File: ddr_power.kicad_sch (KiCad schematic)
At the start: 27 parts, among them U2 MT53D512M32D2DS

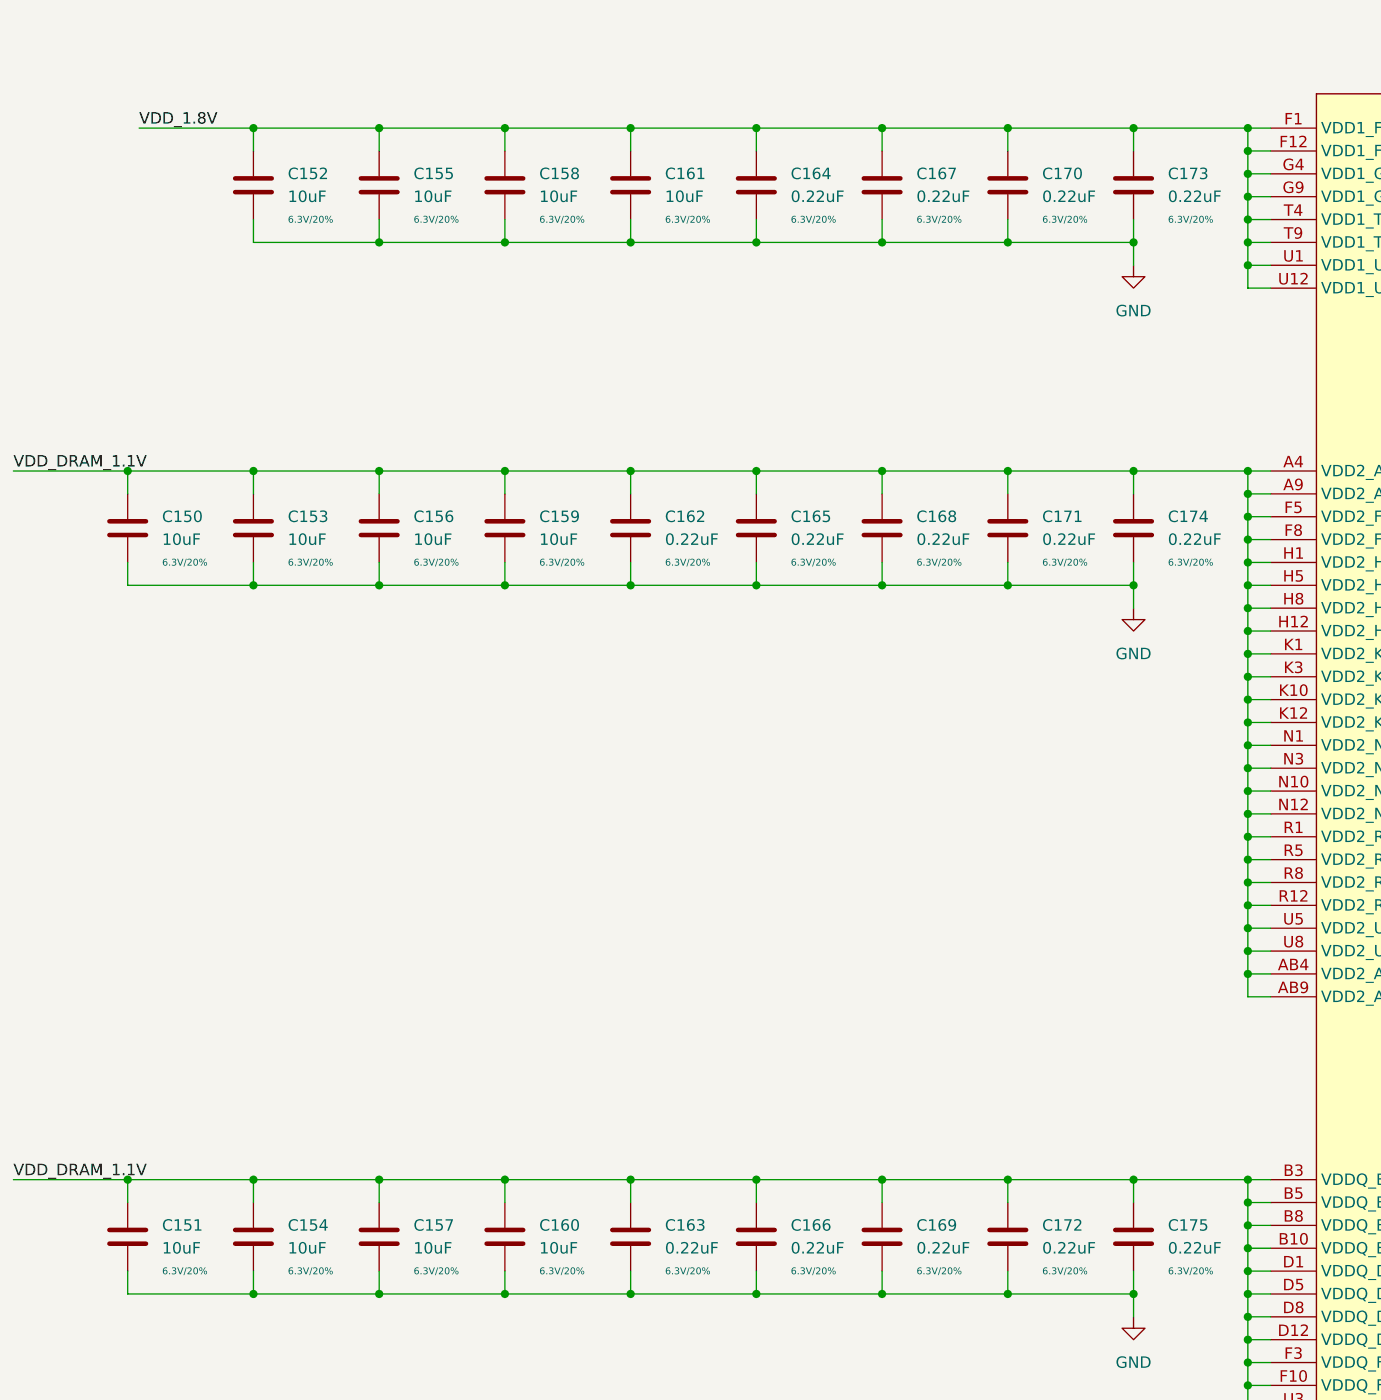
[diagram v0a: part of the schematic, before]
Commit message: add SN65DSI86 DSI2DP ic, SCH, PCB work, flytime work
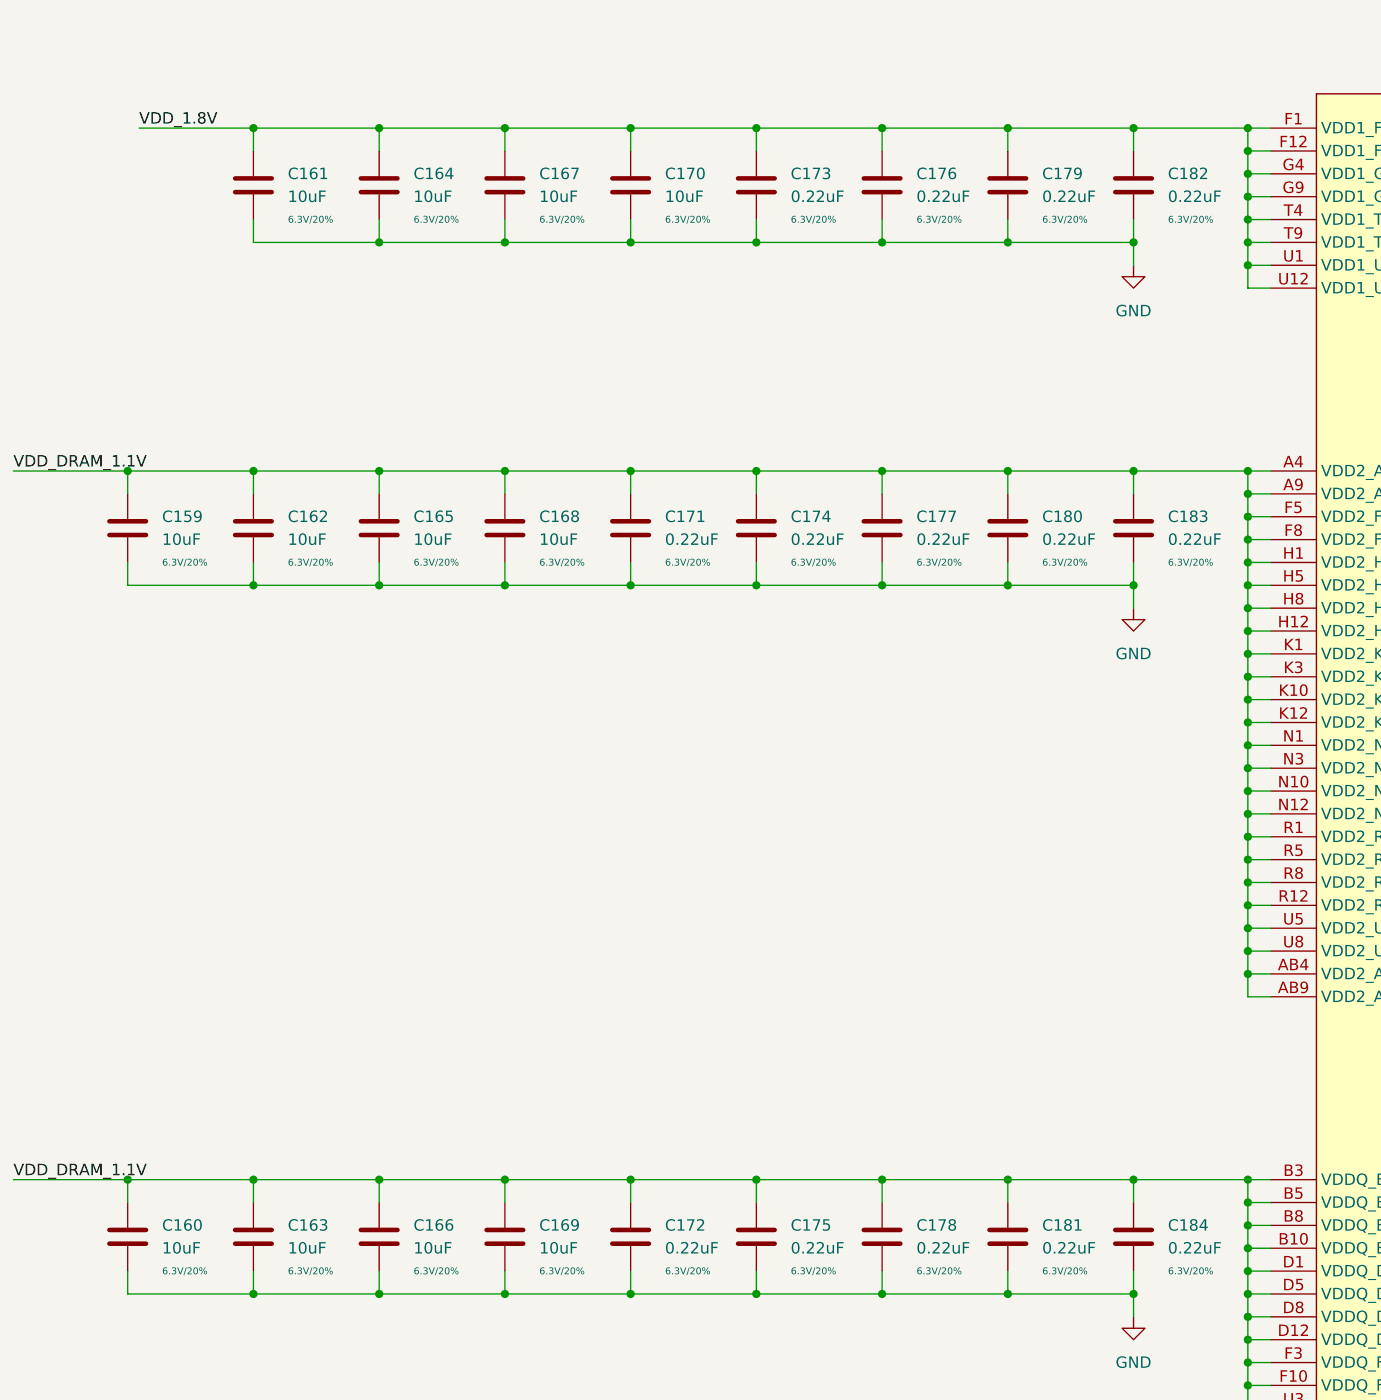
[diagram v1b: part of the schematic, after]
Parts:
- renumbered C150 to C159, C151 to C160, C152 to C161, C153 to C162, C154 to C163, C155 to C164, C156 to C165, C157 to C166, C158 to C167, C159 to C168, C160 to C169, C161 to C170, C162 to C171, C163 to C172, C164 to C173, C165 to C174, C166 to C175, C167 to C176, C168 to C177, C169 to C178, C170 to C179, C171 to C180, C172 to C181, C173 to C182, C174 to C183, C175 to C184
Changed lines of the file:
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@@
   (symbol (lib_id "Device:C") (at 120.65 59.69 0) (unit 1)
     (in_bom yes) (on_board yes)
-    (property "Reference" "C155" (id 0) (at 124.46 58.4199 0)
+    (property "Reference" "C164" (id 0) (at 124.46 58.4199 0)
       (effects (font (size 1.27 1.27)) (justify left))
     )
@@
   (symbol (lib_id "Device:C") (at 190.5 59.69 0) (unit 1)
     (in_bom yes) (on_board yes)
-    (property "Reference" "C170" (id 0) (at 194.31 58.4199 0)
+    (property "Reference" "C179" (id 0) (at 194.31 58.4199 0)
       (effects (font (size 1.27 1.27)) (justify left))
     )
@@
   (symbol (lib_id "Device:C") (at 162.56 97.79 0) (unit 1)
     (in_bom yes) (on_board yes)
-    (property "Reference" "C165" (id 0) (at 166.37 96.5199 0)
+    (property "Reference" "C174" (id 0) (at 166.37 96.5199 0)
       (effects (font (size 1.27 1.27)) (justify left))
     )
@@
   (symbol (lib_id "Device:C") (at 190.5 176.53 0) (unit 1)
     (in_bom yes) (on_board yes)
-    (property "Reference" "C172" (id 0) (at 194.31 175.2599 0)
+    (property "Reference" "C181" (id 0) (at 194.31 175.2599 0)
       (effects (font (size 1.27 1.27)) (justify left))
     )
@@
   (symbol (lib_id "Device:C") (at 148.59 59.69 0) (unit 1)
     (in_bom yes) (on_board yes)
-    (property "Reference" "C161" (id 0) (at 152.4 58.4199 0)
+    (property "Reference" "C170" (id 0) (at 152.4 58.4199 0)
       (effects (font (size 1.27 1.27)) (justify left))
     )
@@
   (symbol (lib_id "Device:C") (at 190.5 97.79 0) (unit 1)
     (in_bom yes) (on_board yes)
-    (property "Reference" "C171" (id 0) (at 194.31 96.5199 0)
+    (property "Reference" "C180" (id 0) (at 194.31 96.5199 0)
       (effects (font (size 1.27 1.27)) (justify left))
     )
@@
   (symbol (lib_id "Device:C") (at 176.53 59.69 0) (unit 1)
     (in_bom yes) (on_board yes)
-    (property "Reference" "C167" (id 0) (at 180.34 58.4199 0)
+    (property "Reference" "C176" (id 0) (at 180.34 58.4199 0)
       (effects (font (size 1.27 1.27)) (justify left))
     )
@@
   (symbol (lib_id "power:GND") (at 204.47 68.58 0) (unit 1)
     (in_bom yes) (on_board yes) (fields_autoplaced)
-    (property "Reference" "#PWR0147" (id 0) (at 204.47 74.93 0)
+    (property "Reference" "#PWR0150" (id 0) (at 204.47 74.93 0)
       (effects (font (size 1.27 1.27)) hide)
     )
@@
   (symbol (lib_id "Device:C") (at 134.62 59.69 0) (unit 1)
     (in_bom yes) (on_board yes)
-    (property "Reference" "C158" (id 0) (at 138.43 58.4199 0)
+    (property "Reference" "C167" (id 0) (at 138.43 58.4199 0)
       (effects (font (size 1.27 1.27)) (justify left))
     )
@@
   (symbol (lib_id "Device:C") (at 204.47 176.53 0) (unit 1)
     (in_bom yes) (on_board yes)
-    (property "Reference" "C175" (id 0) (at 208.28 175.2599 0)
+    (property "Reference" "C184" (id 0) (at 208.28 175.2599 0)
       (effects (font (size 1.27 1.27)) (justify left))
     )
@@
   (symbol (lib_id "Device:C") (at 92.71 176.53 0) (unit 1)
     (in_bom yes) (on_board yes)
-    (property "Reference" "C151" (id 0) (at 96.52 175.2599 0)
+    (property "Reference" "C160" (id 0) (at 96.52 175.2599 0)
       (effects (font (size 1.27 1.27)) (justify left))
     )
@@
   (symbol (lib_id "Device:C") (at 204.47 97.79 0) (unit 1)
     (in_bom yes) (on_board yes)
-    (property "Reference" "C174" (id 0) (at 208.28 96.5199 0)
+    (property "Reference" "C183" (id 0) (at 208.28 96.5199 0)
       (effects (font (size 1.27 1.27)) (justify left))
     )
@@
   (symbol (lib_id "Device:C") (at 204.47 59.69 0) (unit 1)
     (in_bom yes) (on_board yes)
-    (property "Reference" "C173" (id 0) (at 208.28 58.4199 0)
+    (property "Reference" "C182" (id 0) (at 208.28 58.4199 0)
       (effects (font (size 1.27 1.27)) (justify left))
     )
@@
   (symbol (lib_id "Device:C") (at 120.65 97.79 0) (unit 1)
     (in_bom yes) (on_board yes)
-    (property "Reference" "C156" (id 0) (at 124.46 96.5199 0)
+    (property "Reference" "C165" (id 0) (at 124.46 96.5199 0)
       (effects (font (size 1.27 1.27)) (justify left))
     )
@@
   (symbol (lib_id "Device:C") (at 176.53 176.53 0) (unit 1)
     (in_bom yes) (on_board yes)
-    (property "Reference" "C169" (id 0) (at 180.34 175.2599 0)
+    (property "Reference" "C178" (id 0) (at 180.34 175.2599 0)
       (effects (font (size 1.27 1.27)) (justify left))
     )
@@
   (symbol (lib_id "power:GND") (at 204.47 106.68 0) (unit 1)
     (in_bom yes) (on_board yes) (fields_autoplaced)
-    (property "Reference" "#PWR0148" (id 0) (at 204.47 113.03 0)
+    (property "Reference" "#PWR0151" (id 0) (at 204.47 113.03 0)
       (effects (font (size 1.27 1.27)) hide)
     )
@@
   (symbol (lib_id "power:GND") (at 204.47 185.42 0) (unit 1)
     (in_bom yes) (on_board yes) (fields_autoplaced)
-    (property "Reference" "#PWR0149" (id 0) (at 204.47 191.77 0)
+    (property "Reference" "#PWR0152" (id 0) (at 204.47 191.77 0)
       (effects (font (size 1.27 1.27)) hide)
     )
@@
   (symbol (lib_id "Device:C") (at 162.56 59.69 0) (unit 1)
     (in_bom yes) (on_board yes)
-    (property "Reference" "C164" (id 0) (at 166.37 58.4199 0)
+    (property "Reference" "C173" (id 0) (at 166.37 58.4199 0)
       (effects (font (size 1.27 1.27)) (justify left))
     )
@@
   (symbol (lib_id "Device:C") (at 148.59 97.79 0) (unit 1)
     (in_bom yes) (on_board yes)
-    (property "Reference" "C162" (id 0) (at 152.4 96.5199 0)
+    (property "Reference" "C171" (id 0) (at 152.4 96.5199 0)
       (effects (font (size 1.27 1.27)) (justify left))
     )
@@
   (symbol (lib_id "Device:C") (at 106.68 59.69 0) (unit 1)
     (in_bom yes) (on_board yes)
-    (property "Reference" "C152" (id 0) (at 110.49 58.4199 0)
+    (property "Reference" "C161" (id 0) (at 110.49 58.4199 0)
       (effects (font (size 1.27 1.27)) (justify left))
     )
@@
   (symbol (lib_id "power:GND") (at 283.21 200.66 0) (unit 1)
     (in_bom yes) (on_board yes) (fields_autoplaced)
-    (property "Reference" "#PWR0150" (id 0) (at 283.21 207.01 0)
+    (property "Reference" "#PWR0153" (id 0) (at 283.21 207.01 0)
       (effects (font (size 1.27 1.27)) hide)
     )
@@
   (symbol (lib_id "Device:C") (at 106.68 176.53 0) (unit 1)
     (in_bom yes) (on_board yes)
-    (property "Reference" "C154" (id 0) (at 110.49 175.2599 0)
+    (property "Reference" "C163" (id 0) (at 110.49 175.2599 0)
       (effects (font (size 1.27 1.27)) (justify left))
     )
@@
   (symbol (lib_id "Device:C") (at 134.62 176.53 0) (unit 1)
     (in_bom yes) (on_board yes)
-    (property "Reference" "C160" (id 0) (at 138.43 175.2599 0)
+    (property "Reference" "C169" (id 0) (at 138.43 175.2599 0)
       (effects (font (size 1.27 1.27)) (justify left))
     )
@@
   (symbol (lib_id "Device:C") (at 148.59 176.53 0) (unit 1)
     (in_bom yes) (on_board yes)
-    (property "Reference" "C163" (id 0) (at 152.4 175.2599 0)
+    (property "Reference" "C172" (id 0) (at 152.4 175.2599 0)
       (effects (font (size 1.27 1.27)) (justify left))
     )
@@
   (symbol (lib_id "Device:C") (at 134.62 97.79 0) (unit 1)
     (in_bom yes) (on_board yes)
-    (property "Reference" "C159" (id 0) (at 138.43 96.5199 0)
+    (property "Reference" "C168" (id 0) (at 138.43 96.5199 0)
       (effects (font (size 1.27 1.27)) (justify left))
     )
@@
   (symbol (lib_id "Device:C") (at 106.68 97.79 0) (unit 1)
     (in_bom yes) (on_board yes)
-    (property "Reference" "C153" (id 0) (at 110.49 96.5199 0)
+    (property "Reference" "C162" (id 0) (at 110.49 96.5199 0)
       (effects (font (size 1.27 1.27)) (justify left))
     )
@@
   (symbol (lib_id "Device:C") (at 162.56 176.53 0) (unit 1)
     (in_bom yes) (on_board yes)
-    (property "Reference" "C166" (id 0) (at 166.37 175.2599 0)
+    (property "Reference" "C175" (id 0) (at 166.37 175.2599 0)
       (effects (font (size 1.27 1.27)) (justify left))
     )
@@
   (symbol (lib_id "Device:C") (at 120.65 176.53 0) (unit 1)
     (in_bom yes) (on_board yes)
-    (property "Reference" "C157" (id 0) (at 124.46 175.2599 0)
+    (property "Reference" "C166" (id 0) (at 124.46 175.2599 0)
       (effects (font (size 1.27 1.27)) (justify left))
     )
@@
   (symbol (lib_id "Device:C") (at 176.53 97.79 0) (unit 1)
     (in_bom yes) (on_board yes)
-    (property "Reference" "C168" (id 0) (at 180.34 96.5199 0)
+    (property "Reference" "C177" (id 0) (at 180.34 96.5199 0)
       (effects (font (size 1.27 1.27)) (justify left))
     )
@@
   (symbol (lib_id "Device:C") (at 92.71 97.79 0) (unit 1)
     (in_bom yes) (on_board yes)
-    (property "Reference" "C150" (id 0) (at 96.52 96.5199 0)
-      (effects (font (size 1.27 1.27)) (justify left))
-    )
+    (property "Reference" "C159" (id 0) (at 96.52 96.5199 0)
+      (effects (font (size 1.27 1.27)) (justify left))
+    )
